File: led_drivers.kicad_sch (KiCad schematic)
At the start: 22 parts, among them IC1 SamacSys_Parts_HT16K33-28SOP, IC2 SamacSys_Parts_HT16K33-28SOP, SW1 SW_Omron_B3FS, SW2 SW_Omron_B3FS, SW3 SW_Omron_B3FS, SW4 SW_Omron_B3FS

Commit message: Add dc-dc 3.3v to 5v
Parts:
- added C7: 15uF, Capacitor_SMD:C_1210_3225Metric_Pad1.33x2.70mm_HandSolder, symbol Device:C_Small
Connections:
- net +5V: now also C7.2
- net GND: now also C7.1
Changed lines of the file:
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@@
+    (stroke (width 0) (type default))
+  )
+  (wire (pts (xy 119.38 77.47) (xy 119.38 82.55))
     (stroke (width 0) (type default))
   )
@@
   )
   (wire (pts (xy 190.5 90.17) (xy 193.04 90.17))
+    (stroke (width 0) (type default))
+  )
+  (wire (pts (xy 119.38 64.77) (xy 119.38 72.39))
     (stroke (width 0) (type default))
   )
@@
     (property "Intersheetrefs" "${INTERSHEET_REFS}" (at 210.82 90.17 0)
       (effects (font (size 1.27 1.27)) hide)
+    )
+  )
+  (symbol (lib_id "power:GND") (at 119.38 82.55 0) (unit 1)
+    (in_bom yes) (on_board yes) (dnp no)
+    (property "Reference" "#PWR033" (at 119.38 88.9 0)
+      (effects (font (size 1.27 1.27)) hide)
+    )
+    (property "Value" "GND" (at 119.507 86.9442 0)
+      (effects (font (size 1.27 1.27)))
+    )
+    (property "Footprint" "" (at 119.38 82.55 0)
+      (effects (font (size 1.27 1.27)) hide)
+    )
+    (property "Datasheet" "" (at 119.38 82.55 0)
+      (effects (font (size 1.27 1.27)) hide)
+    )
+    (pin "1")
+    (instances
+      (project "LTP305_ESP32_CLOCK"
+        (path "/c007e288-8439-49d9-bbdf-49724c34958c"
+          (reference "#PWR033") (unit 1)
+        )
+      )
+      (project "ltp_kikad"
+        (path "/eed35b77-cbf9-4596-9b17-2558f81058ba"
+          (reference "#PWR09") (unit 1)
+        )
+        (path "/eed35b77-cbf9-4596-9b17-2558f81058ba/eeffdcd2-f49f-4c6e-9443-50950813e7b1"
+          (reference "#PWR035") (unit 1)
+        )
+        (path "/eed35b77-cbf9-4596-9b17-2558f81058ba/7d22e16e-a0ba-4766-b1de-c8cbb28f14f7"
+          (reference "#PWR035") (unit 1)
+        )
+      )
     )
   )
@@
     )
   )
+  (symbol (lib_id "power:+5V") (at 119.38 64.77 0) (unit 1)
+    (in_bom yes) (on_board yes) (dnp no)
+    (property "Reference" "#PWR08" (at 119.38 68.58 0)
+      (effects (font (size 1.27 1.27)) hide)
+    )
+    (property "Value" "+5V" (at 119.761 60.3758 0)
+      (effects (font (size 1.27 1.27)))
+    )
+    (property "Footprint" "" (at 119.38 64.77 0)
+      (effects (font (size 1.27 1.27)) hide)
+    )
+    (property "Datasheet" "" (at 119.38 64.77 0)
+      (effects (font (size 1.27 1.27)) hide)
+    )
+    (pin "1")
+    (instances
+      (project "LTP305_ESP32_CLOCK"
+        (path "/c007e288-8439-49d9-bbdf-49724c34958c"
+          (reference "#PWR08") (unit 1)
+        )
+      )
+      (project "ltp_kikad"
+        (path "/eed35b77-cbf9-4596-9b17-2558f81058ba"
+          (reference "#PWR04") (unit 1)
+        )
+        (path "/eed35b77-cbf9-4596-9b17-2558f81058ba/7d22e16e-a0ba-4766-b1de-c8cbb28f14f7"
+          (reference "#PWR038") (unit 1)
+        )
+      )
+    )
+  )
   (symbol (lib_id "power:GND") (at 147.32 115.57 0) (unit 1)
     (in_bom yes) (on_board yes) (dnp no)
@@
         )
       )
+    )
+  )
+  (symbol (lib_id "Device:C_Small") (at 119.38 74.93 180) (unit 1)
+    (in_bom yes) (on_board yes) (dnp no)
+    (property "Reference" "C7" (at 124.46 73.66 0)
+      (effects (font (size 1.27 1.27)))
+    )
+    (property "Value" "15uF" (at 124.46 76.2 0)
+      (effects (font (size 1.27 1.27)))
+    )
+    (property "Footprint" "Capacitor_SMD:C_1210_3225Metric_Pad1.33x2.70mm_HandSolder" (at 119.38 74.93 0)
+      (effects (font (size 1.27 1.27)) hide)
+    )
+    (property "Datasheet" "~" (at 119.38 74.93 0)
+      (effects (font (size 1.27 1.27)) hide)
+    )
+    (pin "1")
+    (pin "2")
+    (instances
+      (project "LTP305_ESP32_CLOCK"
+        (path "/c007e288-8439-49d9-bbdf-49724c34958c"
+          (reference "C7") (unit 1)
+        )
+      )
+      (project "ltp_kikad"
+        (path "/eed35b77-cbf9-4596-9b17-2558f81058ba"
+          (reference "C6") (unit 1)
+        )
+        (path "/eed35b77-cbf9-4596-9b17-2558f81058ba/eeffdcd2-f49f-4c6e-9443-50950813e7b1"
+          (reference "C10") (unit 1)
+        )
+        (path "/eed35b77-cbf9-4596-9b17-2558f81058ba/7d22e16e-a0ba-4766-b1de-c8cbb28f14f7"
+          (reference "C10") (unit 1)
+        )
+      )

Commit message: Add i2c transciever, Pitanga V2
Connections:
- net SCL renamed 5vSCL
- net SDA renamed 5vSDA
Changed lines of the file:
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@@
     (stroke (width 0) (type default))
   )
-  (global_label "SCL" (shape input) (at 54.61 81.28 180)
+  (global_label "5vSCL" (shape input) (at 54.61 81.28 180)
     (effects (font (size 1.27 1.27)) (justify right))
     (property "Intersheetrefs" "${INTERSHEET_REFS}" (at 48.1966 81.28 0)
@@
     )
   )
-  (global_label "SCL" (shape input) (at 152.4 80.01 180)
+  (global_label "5vSCL" (shape input) (at 152.4 80.01 180)
     (effects (font (size 1.27 1.27)) (justify right))
     (property "Intersheetrefs" "${INTERSHEET_REFS}" (at 145.9866 80.01 0)
@@
     )
   )
-  (global_label "SDA" (shape input) (at 54.61 83.82 180)
+  (global_label "5vSDA" (shape input) (at 54.61 83.82 180)
     (effects (font (size 1.27 1.27)) (justify right))
     (property "Intersheetrefs" "${INTERSHEET_REFS}" (at 54.61 83.82 0)
@@
     )
   )
-  (global_label "SDA" (shape input) (at 152.4 82.55 180)
+  (global_label "5vSDA" (shape input) (at 152.4 82.55 180)
     (effects (font (size 1.27 1.27)) (justify right))
     (property "Intersheetrefs" "${INTERSHEET_REFS}" (at 152.4 82.55 0)

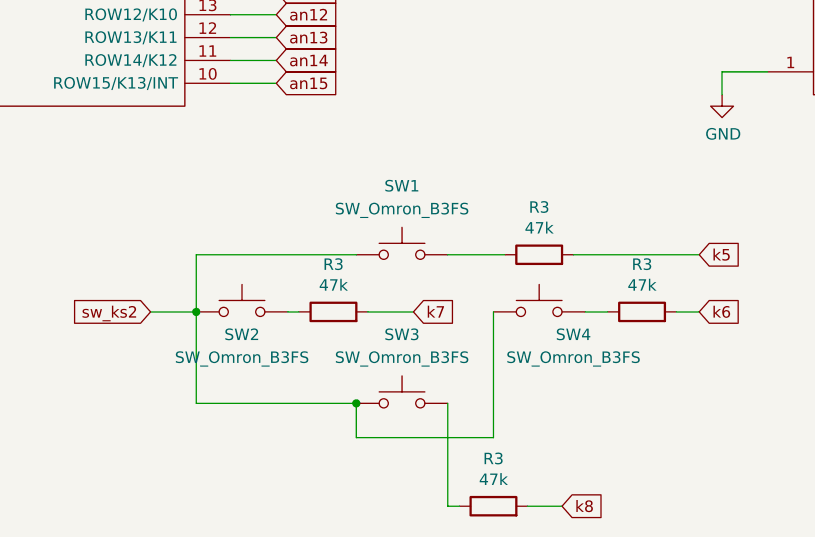
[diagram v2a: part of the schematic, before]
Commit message: Change buttons
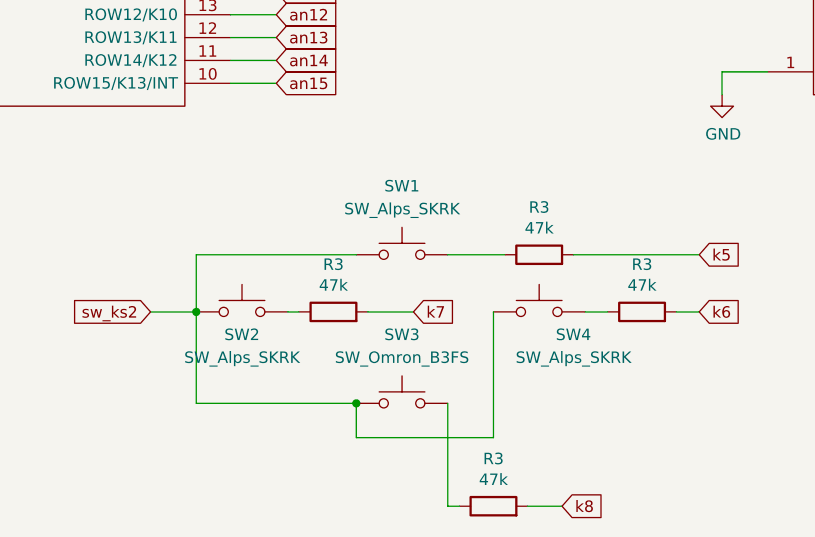
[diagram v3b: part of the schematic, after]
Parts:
- SW1, SW2, SW4: value SW_Omron_B3FS -> SW_Alps_SKRK; footprint Button_Switch_THT:SW_PUSH_6mm_H4.3mm -> Button_Switch_SMD:SW_Push_SPST_NO_Alps_SKRK
- SW3: footprint Button_Switch_THT:SW_PUSH_6mm_H4.3mm -> Button_Switch_SMD:SW_Push_SPST_NO_Alps_SKRK
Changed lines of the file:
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@@
       (effects (font (size 1.27 1.27)))
     )
-    (property "Footprint" "Button_Switch_THT:SW_PUSH_6mm_H4.3mm" (at 111.76 144.78 0)
-      (effects (font (size 1.27 1.27)) hide)
-    )
-    (property "Datasheet" "https://omronfs.omron.com/en_US/ecb/products/pdf/en-b3fs.pdf" (at 111.76 144.78 0)
+    (property "Footprint" "Button_Switch_SMD:SW_Push_SPST_NO_Alps_SKRK" (at 111.76 144.78 0)
+      (effects (font (size 1.27 1.27)) hide)
+    )
+    (property "Datasheet" "" (at 111.76 144.78 0)
       (effects (font (size 1.27 1.27)) hide)
     )
@@
       (effects (font (size 1.27 1.27)))
     )
-    (property "Value" "SW_Omron_B3FS" (at 111.76 128.27 0)
-      (effects (font (size 1.27 1.27)))
-    )
-    (property "Footprint" "Button_Switch_THT:SW_PUSH_6mm_H4.3mm" (at 111.76 128.27 0)
-      (effects (font (size 1.27 1.27)) hide)
-    )
-    (property "Datasheet" "https://omronfs.omron.com/en_US/ecb/products/pdf/en-b3fs.pdf" (at 111.76 128.27 0)
+    (property "Value" "SW_Alps_SKRK" (at 111.76 128.27 0)
+      (effects (font (size 1.27 1.27)))
+    )
+    (property "Footprint" "Button_Switch_SMD:SW_Push_SPST_NO_Alps_SKRK" (at 111.76 128.27 0)
+      (effects (font (size 1.27 1.27)) hide)
+    )
+    (property "Datasheet" "" (at 111.76 128.27 0)
       (effects (font (size 1.27 1.27)) hide)
     )
@@
       (effects (font (size 1.27 1.27)))
     )
-    (property "Value" "SW_Omron_B3FS" (at 130.81 144.78 0)
-      (effects (font (size 1.27 1.27)))
-    )
-    (property "Footprint" "Button_Switch_THT:SW_PUSH_6mm_H4.3mm" (at 127 134.62 0)
-      (effects (font (size 1.27 1.27)) hide)
-    )
-    (property "Datasheet" "https://omronfs.omron.com/en_US/ecb/products/pdf/en-b3fs.pdf" (at 127 134.62 0)
+    (property "Value" "SW_Alps_SKRK" (at 130.81 144.78 0)
+      (effects (font (size 1.27 1.27)))
+    )
+    (property "Footprint" "Button_Switch_SMD:SW_Push_SPST_NO_Alps_SKRK" (at 127 134.62 0)
+      (effects (font (size 1.27 1.27)) hide)
+    )
+    (property "Datasheet" "" (at 127 134.62 0)
       (effects (font (size 1.27 1.27)) hide)
     )
@@
       (effects (font (size 1.27 1.27)))
     )
-    (property "Value" "SW_Omron_B3FS" (at 93.98 144.78 0)
-      (effects (font (size 1.27 1.27)))
-    )
-    (property "Footprint" "Button_Switch_THT:SW_PUSH_6mm_H4.3mm" (at 93.98 134.62 0)
-      (effects (font (size 1.27 1.27)) hide)
-    )
+    (property "Value" "SW_Alps_SKRK" (at 93.98 144.78 0)
+      (effects (font (size 1.27 1.27)))
+    )
+    (property "Footprint" "Button_Switch_SMD:SW_Push_SPST_NO_Alps_SKRK" (at 93.98 134.62 0)
+      (effects (font (size 1.27 1.27)) hide)
+    )
